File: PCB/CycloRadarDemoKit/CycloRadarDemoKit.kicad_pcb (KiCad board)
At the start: 4 copper layers, 60 x 100 mm, 173 parts, among them J101 I2C conn, J102 Radar pins, J103 CAN, J104 100BASE-T1, J105 Radar debug, J301 TMJD0012BENL, J401 ANT_SWD, J601 USB_C_Receptacle_USB2.0, J701 20-16V Supply Voltage, Q501 L8050QLT1G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

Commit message: Logos added
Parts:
- removed the G*** at (202.4, 140.9)
- added G***: LOGO, Socket:FEEC_logo, F.Cu at (170.4, 123.9)
- added G***: LOGO, LOGO, F.Cu at (165.9, 128.4)
- added G***: LOGO, LOGO, B.Cu at (140.8, 96.9)
- added G***: LOGO, Socket:FEEC_logo, B.Cu at (140.9, 103.6)
- REF**: moved to B.Cu
- moved REF** 27.0 mm to (167.8, 144.0), turned to 180 degrees
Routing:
- net /PHY/LED3/PHY_AD3: track 50.4 -> 49.9 mm
- net GNDPWR: vias 23 -> 24
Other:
- board text added: "100BASE-TX"
- board text added: "GPIO"
- board text added: "IN 20-16V"
- board text added: "JLCJLCJLCJLC"
- board text removed: "20-16V Supply Voltage"
- board text removed: "ETH 100BASE-TX"
- board text removed: "r GPIO"

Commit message: start of repair after review
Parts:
- removed REF**: ESD-Logo_8.9x8mm_SilkScreen, Symbol:ESD-Logo_8.9x8mm_SilkScreen
- C705, C708, C804: value 10uF/25V(20%) -> 10uF/50V(20%)
- R201: value 20K(5%) -> 20K(1%)
- R706: value 0.16R(5%) -> 0.18R(5%); footprint Resistor_SMD:R_1210_3225Metric -> Resistor_SMD:R_Shunt_LTR10EVHJLR18
- moved R311 9.77 mm to (117.0, 84.2), turned to -90 degrees
- moved R315 8.69 mm to (118.6, 84.2), turned to -90 degrees
- moved R304 7.99 mm to (135.2, 79.2)
- moved R706 5.61 mm to (125.7, 118.8)
- moved R609 4.65 mm to (124.0, 99.6)
- moved Q701 4.39 mm to (122.1, 119.1)
- moved C312 4.37 mm to (127.5, 74.3), turned to 90 degrees
- moved L701 3.32 mm to (134.8, 128.9)
- moved C703 3.32 mm to (134.1, 125.7)
- moved C705 3.32 mm to (131.0, 121.4)
- moved R709 3.32 mm to (138.2, 120.4)
- moved R711 3.32 mm to (135.1, 120.4)
- moved U702 3.32 mm to (134.5, 123.1)
- moved C704 3.32 mm to (138.5, 124.7)
- moved R705 3.05 mm to (152.5, 128.9)
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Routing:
- net +3V3_PHY: track 81.1 -> 47.8 mm, vias 5 -> 3
- net +3V3: track 198.3 -> 165.9 mm
- net /ESP32/EN_AUTO: track 38.3 -> 52.1 mm, vias 2 -> 0
- net /5V + 3V3/USB 5V: track 45.4 -> 32.6 mm
- net /USB/IN_5V: track 14.8 -> 3.24 mm
- net /PHY/LED3/PHY_AD3: track 49.9 -> 38.4 mm, vias 4 -> 2
- net Net-(J601-CC1): track 11.0 -> 0.00 mm
- net +5V: track 313.1 -> 303.7 mm, vias 13 -> 12
- net /20V + 12V/Battery 5V: track 56.3 -> 63.6 mm
- net /ESP32/12V_DIS: track 127.2 -> 133.8 mm
- net Net-(D506-DOUT): track 72.5 -> 66.6 mm
- net /20V + 12V/20V_HS: track 22.2 -> 28.0 mm
- net Net-(J301-Pad10): track 7.90 -> 3.04 mm
- net /20V + 12V/12V_HS: track 28.8 -> 33.6 mm
- net /USB/DP: track 17.3 -> 12.9 mm
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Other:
- board text added: "20-16V"
- board text added: "ETH 1000BASE-T1"
- board text added: "H"
- board text added: "L"
- board text added: "POLYGON"
- board text added: "T+"
- board text added: "T-"
- board text removed: "ETH 100BASE-T1"
- board text removed: "IN 20-16V"

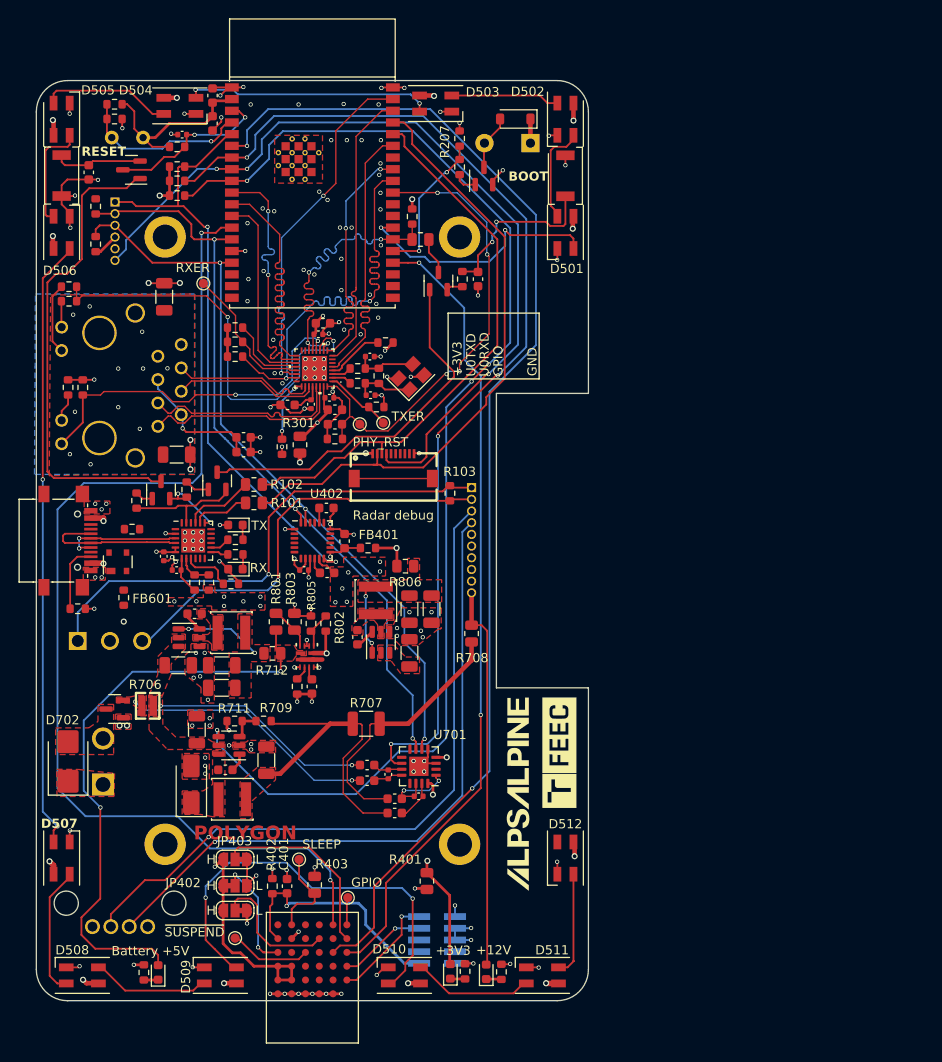
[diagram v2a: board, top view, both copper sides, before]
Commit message: Review changes WIP, USB ESD changed, MDIC pullup added
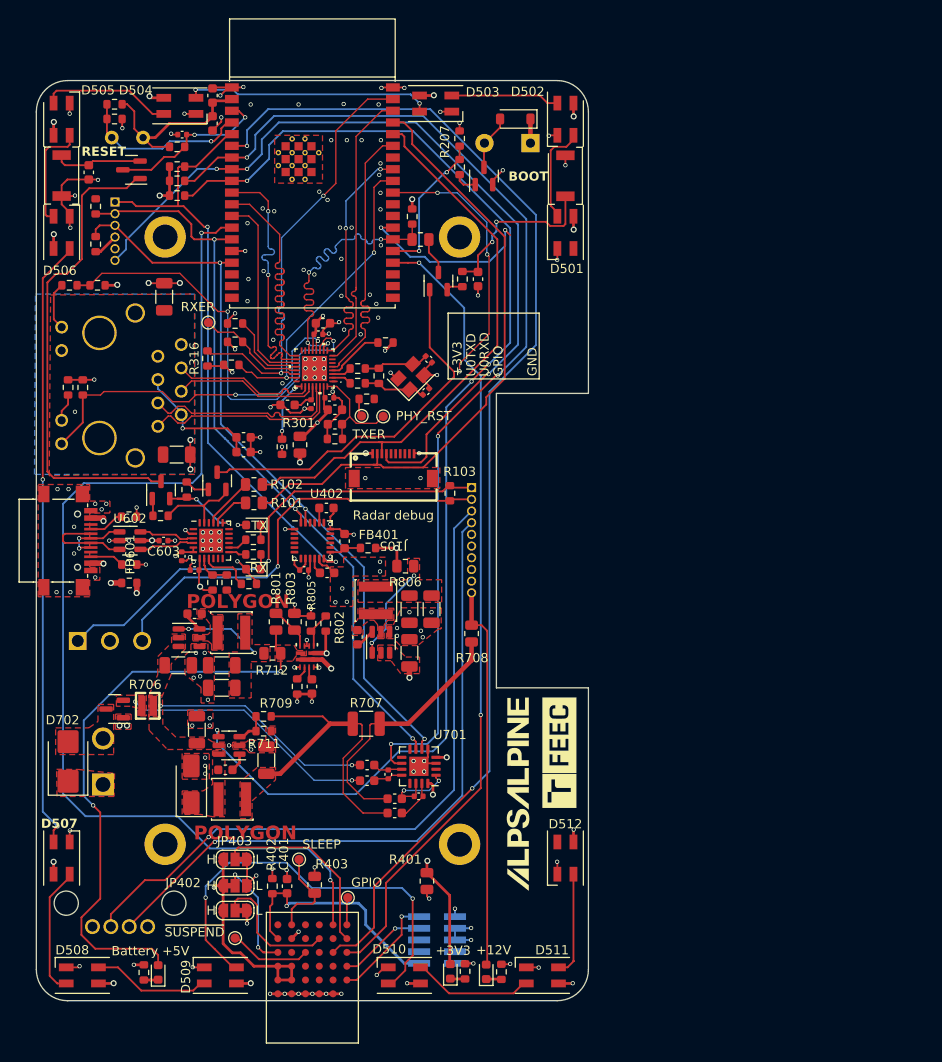
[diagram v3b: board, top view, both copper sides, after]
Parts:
- removed D603: SP0503BAHT, Package_TO_SOT_SMD:SOT-143
- added C603: 100nF, Capacitor_SMD:C_0402_1005Metric, F.Cu at (127.4, 100.8)
- added R316: 5.1K(1%), Resistor_SMD:R_0603_1608Metric, F.Cu at (132.2, 81.0)
- added U602: USBLC6-2SC6, Package_TO_SOT_SMD:SOT-23-6, F.Cu at (123.7, 100.8)
- moved R608 7.38 mm to (123.7, 103.4)
- moved C309 6.41 mm to (156.2, 81.1), turned to -45 degrees
- moved C308 6.04 mm to (155.9, 84.6), turned to 45 degrees
- moved TP303 4.29 mm to (132.2, 77.1)
- moved R711 3.34 mm to (138.2, 121.5), turned to 0 degrees
- moved R309 3.10 mm to (120.2, 73.1), turned to 0 degrees
- moved R604 3.08 mm to (127.0, 98.1), turned to 180 degrees
- moved TP301 2.69 mm to (151.2, 87.3)
- moved TP302 2.47 mm to (148.9, 87.3)
- moved R601 1.95 mm to (136.7, 105.5)
- moved U601 1.95 mm to (132.6, 100.8)
- moved C601 1.95 mm to (129.3, 102.5)
- moved C602 1.95 mm to (130.8, 104.0)
- moved D601 1.95 mm to (137.1, 99.1)
- moved D602 1.95 mm to (137.1, 103.9)
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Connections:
- net /USB/IN_5V renamed /USB/VBUS_IN
- J601 pad A6: /USB/DP -> /USB/DIP
- J601 pad A7: /USB/DN -> /USB/DIN
- J601 pad B6: /USB/DP -> /USB/DIP
- J601 pad B7: /USB/DN -> /USB/DIN
- J601 pad S1: unconnected-(J601-SHIELD-PadS1) -> GND
- U601 pad 3: /USB/DP -> /USB/DOP
- U601 pad 4: /USB/DN -> /USB/DON
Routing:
- net +5V: track 303.7 -> 25.7 mm, vias 12 -> 14
- net /IMU + ANT/VCC: track 54.9 -> 26.2 mm
- net /5V + 3V3/USB 5V: track 32.6 -> 9.76 mm, vias 2 -> 3
- net /USB/DN: track 16.1 -> 0.00 mm
- net /MAC_MDIO: track 47.3 -> 33.8 mm
- net /USB/DP: track 12.9 -> 0.00 mm, vias 2 -> 0
- net +3V3_USB: track 18.1 -> 6.98 mm
- net /PHY_RST: track 52.3 -> 41.3 mm, vias 4 -> 3
- net /USB/DIN: track 0.00 -> 10.2 mm
- net /MAC_MDC: track 39.0 -> 48.0 mm
- net unconnected-(J105-PadNC): track 8.50 -> 0.00 mm
- net /ESP32/LED: track 27.6 -> 19.5 mm
- net /USB/DIP: track 0.00 -> 7.09 mm, vias 0 -> 2
- net /USB/DOP: track 0.00 -> 6.11 mm
- net /USB/DON: track 0.00 -> 6.11 mm
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- added copper zone on In2.Cu, net +3V3_USB
- added copper zone on In2.Cu, net +5V
- added copper zone on In2.Cu, net /5V + 3V3/USB 5V
- added copper zone on In2.Cu, net /IMU + ANT/VCC
- added copper zone on In2.Cu, net /USB/VBUS_IN

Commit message: ready for 2. review
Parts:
- C302: footprint Capacitor_SMD:C_0603_1608Metric -> Capacitor_SMD:C_0402_1005Metric
- moved C311 4.31 mm to (131.8, 90.3), turned to -90 degrees
- moved C310 2.72 mm to (133.4, 90.3), turned to -90 degrees
- moved C302 2.68 mm to (142.1, 77.6), turned to 0 degrees
- moved R713 2.61 mm to (127.8, 147.6)
- moved C303 2.16 mm to (142.1, 78.6), turned to 180 degrees
- moved R316 1.02 mm to (132.3, 80.0)
- moved R201 0.65 mm to (155.1, 65.5)
- moved D704 0.55 mm to (126.2, 147.6)
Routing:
- net +3V3: track 165.9 -> 75.4 mm, vias 8 -> 10
- net +5V: track 25.7 -> 56.7 mm
- net +3V3_PHY: track 43.9 -> 25.1 mm, vias 7 -> 9
- net /Radar_GPIO: track 91.1 -> 81.1 mm
- net /ESP32/PMIC_INT: track 114.2 -> 105.2 mm, vias 4 -> 2
- net /ESP32/12V_DIS: track 133.8 -> 124.8 mm, vias 4 -> 2
- net /ESP32/LED: track 19.5 -> 27.2 mm
- net /IMU_INT: track 66.9 -> 73.7 mm, vias 2 -> 3
- net Net-(D501-DOUT): track 10.9 -> 16.5 mm
- net /ESP32/U1RXD: track 130.8 -> 126.7 mm
- net Net-(J301-RCT): track 14.2 -> 10.7 mm
- net Net-(U301-TXER/FXSD): track 2.47 -> 5.66 mm
- net /ESP32/U1RTS: track 116.1 -> 118.9 mm, vias 2 -> 4
- net /PHY_RST: track 41.3 -> 38.9 mm, vias 3 -> 2
- net GND: track 137.8 -> 135.8 mm, vias 172 -> 195
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- added copper zone on In2.Cu, net +3V3
- added copper zone on In2.Cu, net +3V3_PHY
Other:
- board text added: "1000BASE-T1"
- board text added: "SWDCLK"
- board text added: "SWDIO"
- board text added: "~{RST}"
- board text removed: "ETH 1000BASE-T1"
- board text removed: "POLYGON"

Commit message: PCB finished and reviewed
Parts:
- added REF**: ESD-Logo_8.9x8mm_SilkScreen, Symbol:ESD-Logo_8.9x8mm_SilkScreen, B.Cu at (168.3, 121.9)
- moved R707 5.92 mm to (143.9, 123.0), turned to 90 degrees
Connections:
- H101 pad 1: (no net) -> GND
- H102 pad 1: (no net) -> GND
- H103 pad 1: (no net) -> GND
- H104 pad 1: (no net) -> GND
- R709 pad 1: /20V + 12V/12V_HS -> /20V + 12V/12V_LS
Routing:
- net /20V + 12V/12V_HS: track 33.9 -> 20.2 mm
- net /20V + 12V/12V_LS: track 29.0 -> 41.5 mm
- net +3V3: track 75.4 -> 81.9 mm
- net GND: track 135.8 -> 139.1 mm, vias 195 -> 186
- net /USB/DIN: track 10.2 -> 7.87 mm
- net Net-(C205-Pad1): track 17.4 -> 18.9 mm
- net /ESP32/12V_DIS: track 124.8 -> 124.0 mm
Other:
- board text added: "RSS development & demonstration module"
- board text removed: "4.6mm D52 6.7mm ESP Edge R=4mm"

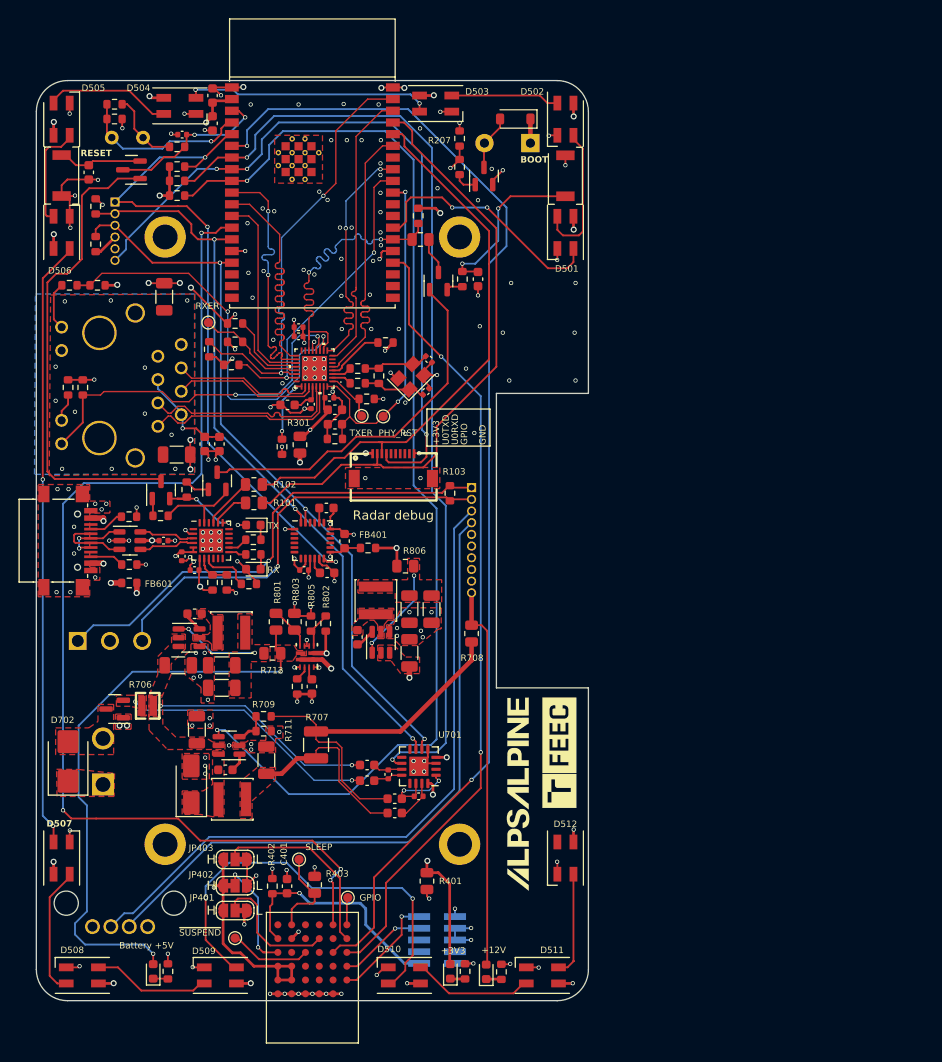
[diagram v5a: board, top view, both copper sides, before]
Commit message: JLCPCB mistakes repaired, cosmetics on PCB
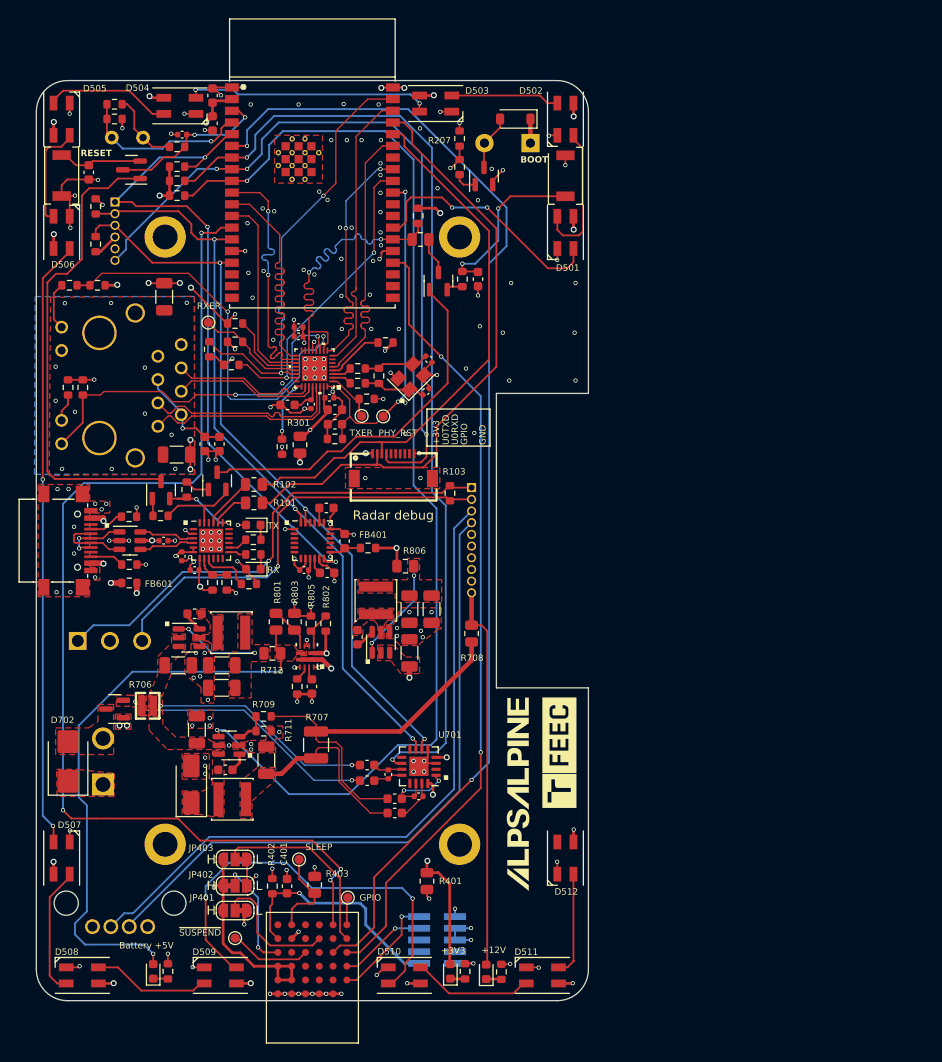
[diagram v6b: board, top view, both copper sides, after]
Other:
- board text added: "."
- board text added: "Designed by MT"

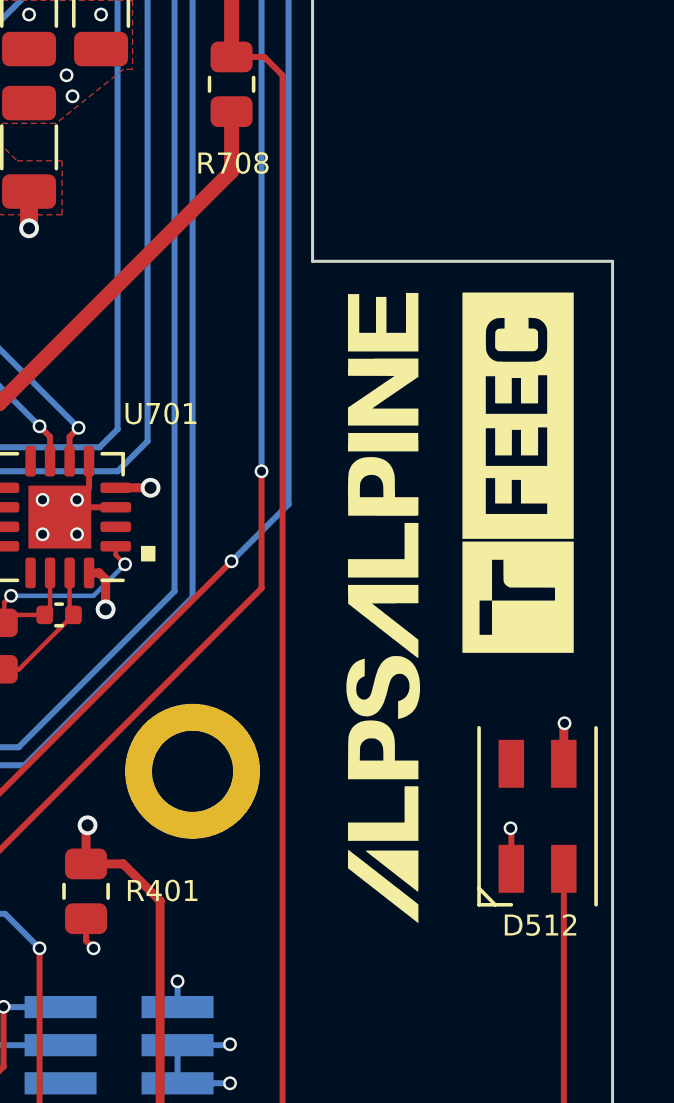
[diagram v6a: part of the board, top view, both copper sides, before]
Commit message: Sematic Versioning implemented, whish list added
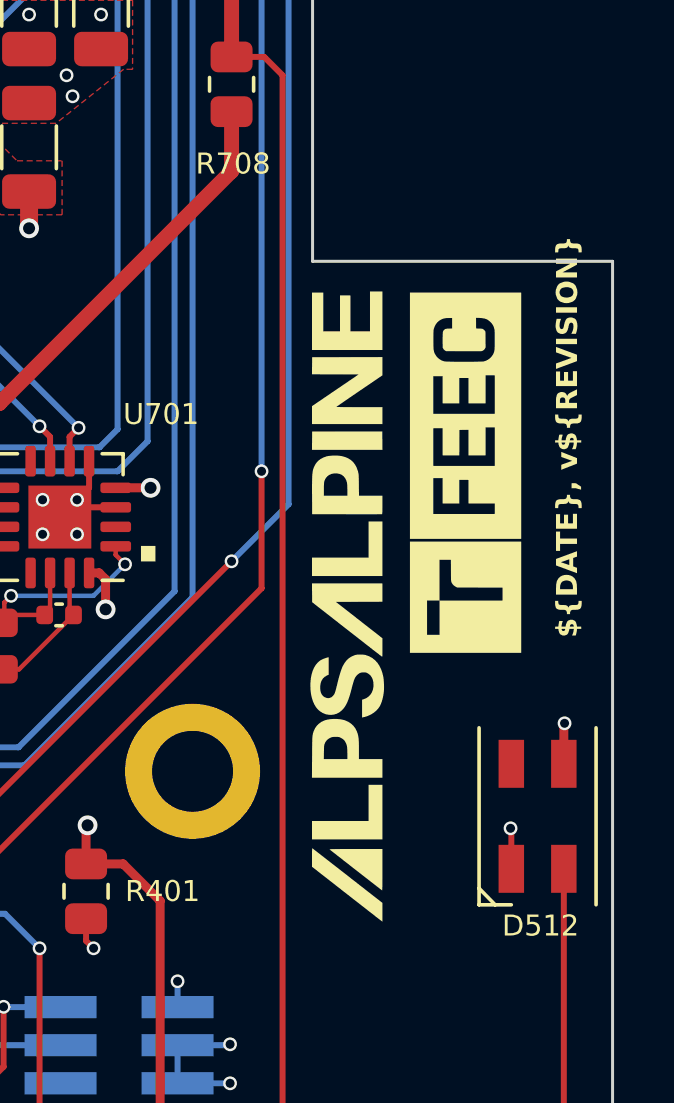
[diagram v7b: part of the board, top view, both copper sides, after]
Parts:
- moved G*** 1.75 mm to (168.7, 123.9)
- moved G*** 1.20 mm to (164.7, 128.3)
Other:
- board text added: "${DATE}, v${REVISION}"
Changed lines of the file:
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@@
   )
   (paper "A4")
+  (title_block
+    (title "${TITLE}")
+    (date "${DATE}")
+    (rev "${REVISION}")
+    (company "${COMPANY}")
+    (comment 1 "${CREATOR}")
+    (comment 2 "${APPROVER}")
+    (comment 3 "${STATUS}")
+    (comment 4 "${LANG}")
+    (comment 5 "${NOTE}")
+  )
   (layers
     (0 "F.Cu" signal)
@@
     )
   )
+  (property "APPROVER" "J. Giertl")
+  (property "COMPANY" "ALPS Electric Czech, s.r.o.")
+  (property "CREATOR" "M. Tavoda")
+  (property "DATE" "2024-01-29")
+  (property "LANG" "EN")
+  (property "NOTE" "")
+  (property "REVISION" "1.0.0")
+  (property "STATUS" "FINAL")
+  (property "SUBTITLE" "RSS development & demonstration module")
+  (property "TITLE" "Radar Safety Sensor ")
   (net 0 "")
   (net 1 "/5V + 3V3/USB 5V")
@@
   )
   (footprint "Socket:FEEC_logo" (layer "F.Cu")
-    (at 170.4 123.875 90)
+    (at 168.65 123.875 90)
     (attr board_only exclude_from_pos_files exclude_from_bom)
     (fp_text reference "G***" (at 0 0 90 unlocked) (layer "F.SilkS") hide
@@
   )
   (footprint "LOGO" (layer "F.Cu")
-    (at 165.9 128.375 90)
+    (at 164.7 128.325 90)
     (attr board_only exclude_from_pos_files exclude_from_bom)
     (fp_text reference "G***" (at 0 0 90 unlocked) (layer "F.SilkS") hide
@@
     (effects (font (size 1.5 1.5) (thickness 0.2) bold) (justify left bottom mirror))
   )
+  (gr_text "${DATE}, v${REVISION}" (at 146.598842 111.775) (layer "B.SilkS")
+    (effects (font (size 0.7 0.7) (thickness 0.16) bold) (justify left bottom mirror))
+  )
   (gr_text "GND" (at 162.75 143.025) (layer "B.SilkS")
     (effects (font (size 1 1) (thickness 0.153)) (justify mirror))
@@
     (effects (font (size 0.7 0.7) (thickness 0.16)) (justify left))
   )
+  (gr_text "${DATE}, v${REVISION}" (at 172.45 129.375 90) (layer "F.SilkS")
+    (effects (font (size 0.7 0.7) (thickness 0.16) bold) (justify left bottom))
+  )
   (gr_text "RX" (at 138.65 104.425) (layer "F.SilkS")
